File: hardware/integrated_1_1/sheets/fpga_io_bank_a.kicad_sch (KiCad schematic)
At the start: 12 parts, among them SW3 DNF, U2 XC6SLX9-TQG144, U4 XLH335200.000000I, U5 NC7SZ125M5X

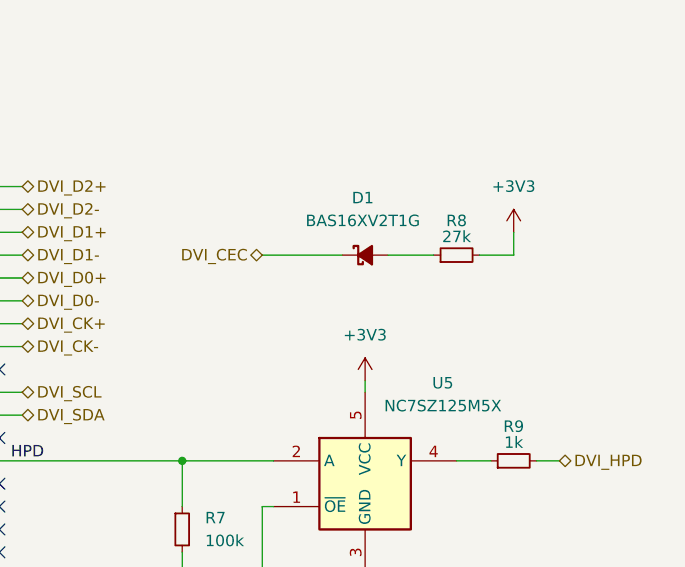
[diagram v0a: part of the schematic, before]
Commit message: implemented changes as suggested by https://github.com/diminDDL
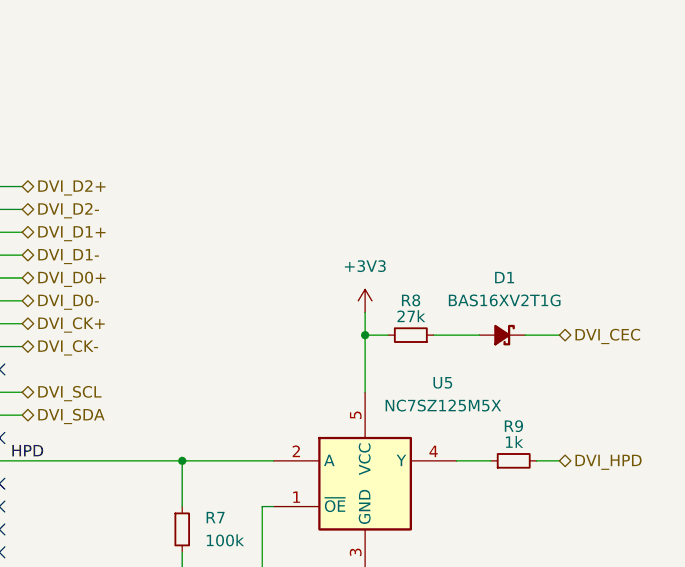
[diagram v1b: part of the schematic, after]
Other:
- moved on the sheet: D1, R8
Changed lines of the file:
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@@
+	)
+	(junction
+		(at 217.17 97.79)
+		(diameter 0)
+		(color 0 0 0 0)
 	)
 	(junction
@@
 	(wire
 		(pts
-			(xy 217.17 102.87) (xy 217.17 104.14)
-		)
-		(stroke
-			(width 0)
-			(type default)
-		)
-	)
-	(wire
-		(pts
 			(xy 179.07 86.36) (xy 176.53 86.36)
 		)
@@
 	(wire
 		(pts
-			(xy 205.74 88.9) (xy 214.63 88.9)
+			(xy 238.76 97.79) (xy 234.95 97.79)
 		)
 		(stroke
@@
 	(wire
 		(pts
-			(xy 233.68 86.36) (xy 233.68 88.9)
-		)
-		(stroke
-			(width 0)
-			(type default)
-		)
-	)
-	(wire
-		(pts
 			(xy 90.17 58.42) (xy 87.63 58.42)
 		)
@@
 	(wire
 		(pts
+			(xy 217.17 97.79) (xy 217.17 104.14)
+		)
+		(stroke
+			(width 0)
+			(type default)
+		)
+	)
+	(wire
+		(pts
 			(xy 50.8 104.14) (xy 74.93 104.14)
 		)
@@
 	(wire
 		(pts
-			(xy 219.71 88.9) (xy 224.79 88.9)
+			(xy 229.87 97.79) (xy 224.79 97.79)
 		)
 		(stroke
@@
 	(wire
 		(pts
+			(xy 219.71 97.79) (xy 217.17 97.79)
+		)
+		(stroke
+			(width 0)
+			(type default)
+		)
+	)
+	(wire
+		(pts
 			(xy 85.09 48.26) (xy 85.09 50.8)
 		)
@@
 	(wire
 		(pts
-			(xy 233.68 88.9) (xy 229.87 88.9)
-		)
-		(stroke
-			(width 0)
-			(type default)
-		)
-	)
-	(wire
-		(pts
 			(xy 176.53 134.62) (xy 179.07 134.62)
 		)
@@
 		(pts
 			(xy 166.37 58.42) (xy 166.37 60.96)
+		)
+		(stroke
+			(width 0)
+			(type default)
+		)
+	)
+	(wire
+		(pts
+			(xy 217.17 95.25) (xy 217.17 97.79)
 		)
 		(stroke
@@
 	(hierarchical_label "DVI_CEC"
 		(shape bidirectional)
-		(at 205.74 88.9 180)
+		(at 238.76 97.79 0)
 		(fields_autoplaced yes)
 		(effects
@@
 				(size 1.27 1.27)
 			)
-			(justify right)
+			(justify left)
 		)
 	)
@@
 	(symbol
 		(lib_id "Device:R_Small")
-		(at 227.33 88.9 90)
+		(at 222.25 97.79 270)
+		(mirror x)
 		(unit 1)
 		(exclude_from_sim no)
@@
 		(dnp no)
 		(property "Reference" "R8"
-			(at 227.33 85.09 90)
+			(at 222.25 93.98 90)
 			(effects
 				(font
@@
 		)
 		(property "Value" "27k"
-			(at 227.33 86.868 90)
+			(at 222.25 95.758 90)
 			(effects
 				(font
@@
 		)
 		(property "Footprint" "KiCAD Library:R_0402_1005Metric"
-			(at 227.33 88.9 0)
+			(at 222.25 97.79 0)
 			(effects
 				(font
@@
 		)
 		(property "Datasheet" "~"
-			(at 227.33 88.9 0)
+			(at 222.25 97.79 0)
 			(effects
 				(font
@@
 		)
 		(property "Description" "Resistor, small symbol"
-			(at 227.33 88.9 0)
+			(at 222.25 97.79 0)
 			(effects
 				(font
@@
 	(symbol
 		(lib_id "Device:D_Schottky_Small_Filled")
-		(at 217.17 88.9 0)
+		(at 232.41 97.79 0)
+		(mirror y)
 		(unit 1)
 		(exclude_from_sim no)
@@
 		(fields_autoplaced yes)
 		(property "Reference" "D1"
-			(at 216.916 82.55 0)
+			(at 232.664 91.44 0)
 			(effects
 				(font
@@
 		)
 		(property "Value" "BAS16XV2T1G"
-			(at 216.916 85.09 0)
+			(at 232.664 93.98 0)
 			(effects
 				(font
@@
 		)
 		(property "Footprint" "Diode_SMD:D_SOD-523"
-			(at 217.17 88.9 90)
+			(at 232.41 97.79 90)
 			(effects
 				(font
@@
 		)
 		(property "Datasheet" "~"
-			(at 217.17 88.9 90)
+			(at 232.41 97.79 90)
 			(effects
 				(font
@@
 		)
 		(property "Description" "Schottky diode, small symbol, filled shape"
-			(at 217.17 88.9 0)
+			(at 232.41 97.79 0)
 			(effects
 				(font
@@
 		(lib_name "+3V3_1")
 		(lib_id "power:+3V3")
-		(at 217.17 102.87 0)
+		(at 217.17 95.25 0)
 		(unit 1)
 		(exclude_from_sim no)
@@
 		(fields_autoplaced yes)
 		(property "Reference" "#PWR030"
-			(at 217.17 106.68 0)
+			(at 217.17 99.06 0)
 			(effects
 				(font
@@
 		)
 		(property "Value" "+3V3"
-			(at 217.17 97.79 0)
+			(at 217.17 90.17 0)
 			(effects
 				(font
@@
 		)
 		(property "Footprint" ""
-			(at 217.17 102.87 0)
+			(at 217.17 95.25 0)
 			(effects
 				(font
@@
 		)
 		(property "Datasheet" ""
-			(at 217.17 102.87 0)
+			(at 217.17 95.25 0)
 			(effects
 				(font
@@
 		)
 		(property "Description" "Power symbol creates a global label with name \"+3V3\""
-			(at 217.17 102.87 0)
+			(at 217.17 95.25 0)
 			(effects
 				(font
@@
 					(unit 1)
 				)
-			)
-		)
-	)
-	(symbol
-		(lib_name "+3V3_1")
-		(lib_id "power:+3V3")
-		(at 233.68 86.36 0)
-		(unit 1)
-		(exclude_from_sim no)
-		(in_bom yes)
-		(on_board yes)
-		(dnp no)
-		(fields_autoplaced yes)
-		(property "Reference" "#PWR031"
-			(at 233.68 90.17 0)
-			(effects
-				(font
-					(size 1.27 1.27)
-				)
-				(hide yes)
-			)
-		)
-		(property "Value" "+3V3"
-			(at 233.68 81.28 0)
-			(effects
-				(font
-					(size 1.27 1.27)
-				)
-			)
-		)
-		(property "Footprint" ""
-			(at 233.68 86.36 0)
-			(effects
-				(font
-					(size 1.27 1.27)
-				)
-				(hide yes)
-			)
-		)
-		(property "Datasheet" ""
-			(at 233.68 86.36 0)
-			(effects
-				(font
-					(size 1.27 1.27)
-				)
-				(hide yes)
-			)
-		)
-		(property "Description" "Power symbol creates a global label with name \"+3V3\""
-			(at 233.68 86.36 0)
-			(effects
-				(font
-					(size 1.27 1.27)
-				)
-				(hide yes)
-			)
-		)
-		(pin "1"
-		)
-		(instances
-			(project "integrated"
-				(path "/5cc60e42-d666-4a43-b4f0-3784ee4bf951/abc66463-55c0-4aba-9f8d-f6d711d3ef5b"
-					(reference "#PWR031")
-					(unit 1)
-				)
